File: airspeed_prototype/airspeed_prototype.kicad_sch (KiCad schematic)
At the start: 6 parts, among them J1 Conn_01x03_Pin, J3 Conn_01x06_Pin, J4 Conn_01x08_Pin, U1 ESP32-DevKitC

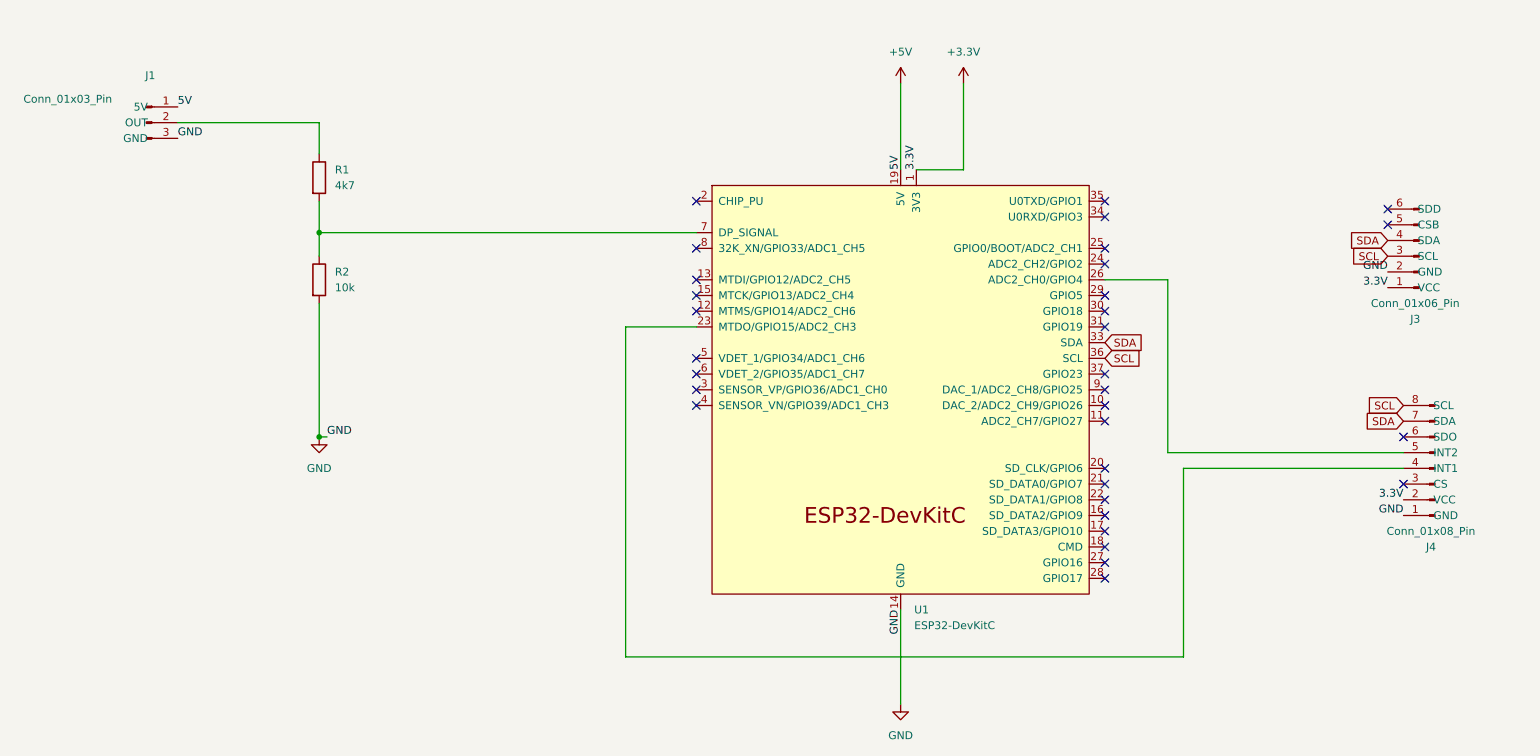
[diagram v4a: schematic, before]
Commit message: new pcb layout
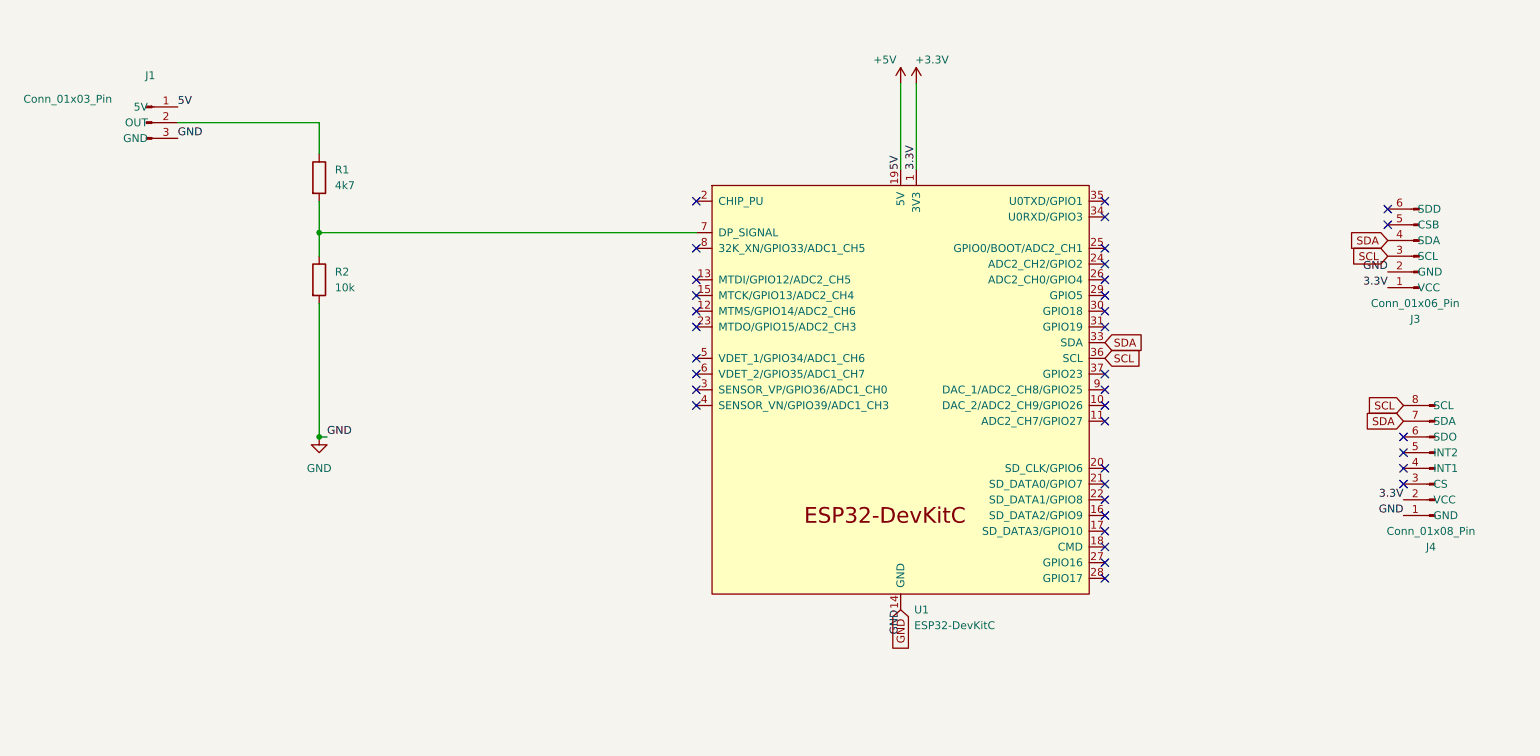
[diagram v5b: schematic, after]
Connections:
- net at U1.23 (MTDO/GPIO15/ADC2_CH3): no longer J4.4 (INT1)
- net at U1.26 (ADC2_CH0/GPIO4): no longer J4.5 (INT2)
- no-connect marks 32 -> 36
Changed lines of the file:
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@@
   (no_connect (at 129.54 50.8))
   (no_connect (at 195.58 86.36))
+  (no_connect (at 129.54 71.12))
   (no_connect (at 129.54 58.42))
   (no_connect (at 129.54 63.5))
   (no_connect (at 195.58 99.06))
+  (no_connect (at 243.84 91.44))
   (no_connect (at 243.84 96.52))
   (no_connect (at 241.3 54.61))
@@
   (no_connect (at 195.58 68.58))
   (no_connect (at 195.58 53.34))
+  (no_connect (at 243.84 93.98))
   (no_connect (at 195.58 109.22))
   (no_connect (at 195.58 104.14))
@@
   (no_connect (at 195.58 96.52))
   (no_connect (at 195.58 50.8))
+  (no_connect (at 195.58 63.5))
   (no_connect (at 195.58 60.96))
   (no_connect (at 195.58 111.76))
@@
     (stroke (width 0) (type default))
   )
-  (wire (pts (xy 208.28 124.46) (xy 118.11 124.46))
-    (stroke (width 0) (type default))
-  )
   (wire (pts (xy 129.54 55.88) (xy 68.58 55.88))
     (stroke (width 0) (type default))
   )
-  (wire (pts (xy 162.56 116.84) (xy 162.56 132.08))
-    (stroke (width 0) (type default))
-  )
   (wire (pts (xy 69.85 88.9) (xy 68.58 88.9))
     (stroke (width 0) (type default))
   )
-  (wire (pts (xy 243.84 91.44) (xy 205.74 91.44))
-    (stroke (width 0) (type default))
-  )
-  (wire (pts (xy 172.72 31.75) (xy 172.72 45.72))
-    (stroke (width 0) (type default))
-  )
-  (wire (pts (xy 205.74 91.44) (xy 205.74 63.5))
-    (stroke (width 0) (type default))
-  )
-  (wire (pts (xy 208.28 93.98) (xy 208.28 124.46))
+  (wire (pts (xy 165.1 31.75) (xy 165.1 45.72))
     (stroke (width 0) (type default))
   )
@@
     (stroke (width 0) (type default))
   )
-  (wire (pts (xy 172.72 45.72) (xy 165.1 45.72))
-    (stroke (width 0) (type default))
-  )
   (wire (pts (xy 68.58 50.8) (xy 68.58 55.88))
-    (stroke (width 0) (type default))
-  )
-  (wire (pts (xy 195.58 63.5) (xy 205.74 63.5))
-    (stroke (width 0) (type default))
-  )
-  (wire (pts (xy 118.11 124.46) (xy 118.11 71.12))
-    (stroke (width 0) (type default))
-  )
-  (wire (pts (xy 243.84 93.98) (xy 208.28 93.98))
-    (stroke (width 0) (type default))
-  )
-  (wire (pts (xy 118.11 71.12) (xy 129.54 71.12))
     (stroke (width 0) (type default))
   )
@@
     (property "Intersheetrefs" "${INTERSHEET_REFS}" (at 202.0728 76.2 0)
       (effects (font (size 1.27 1.27)) (justify left) hide)
+    )
+  )
+  (global_label "GND" (shape input) (at 162.56 116.84 270) (fields_autoplaced)
+    (effects (font (size 1.27 1.27)) (justify right))
+    (property "Intersheetrefs" "${INTERSHEET_REFS}" (at 162.56 123.6957 90)
+      (effects (font (size 1.27 1.27)) (justify right) hide)
     )
   )
@@
     )
   )
-  (symbol (lib_id "power:+3.3V") (at 172.72 31.75 0) (unit 1)
+  (symbol (lib_id "power:+3.3V") (at 165.1 31.75 0) (unit 1)
     (in_bom yes) (on_board yes) (dnp no)
-    (property "Reference" "#PWR04" (at 172.72 35.56 0)
-      (effects (font (size 1.27 1.27)) hide)
-    )
-    (property "Value" "+3.3V" (at 172.72 26.67 0)
-      (effects (font (size 1.27 1.27)))
-    )
-    (property "Footprint" "" (at 172.72 31.75 0)
-      (effects (font (size 1.27 1.27)) hide)
-    )
-    (property "Datasheet" "" (at 172.72 31.75 0)
+    (property "Reference" "#PWR04" (at 165.1 35.56 0)
+      (effects (font (size 1.27 1.27)) hide)
+    )
+    (property "Value" "+3.3V" (at 167.64 27.94 0)
+      (effects (font (size 1.27 1.27)))
+    )
+    (property "Footprint" "" (at 165.1 31.75 0)
+      (effects (font (size 1.27 1.27)) hide)
+    )
+    (property "Datasheet" "" (at 165.1 31.75 0)
       (effects (font (size 1.27 1.27)) hide)
     )
@@
   )
   (symbol (lib_id "power:+5V") (at 162.56 31.75 0) (unit 1)
-    (in_bom yes) (on_board yes) (dnp no) (fields_autoplaced)
+    (in_bom yes) (on_board yes) (dnp no)
     (property "Reference" "#PWR03" (at 162.56 35.56 0)
       (effects (font (size 1.27 1.27)) hide)
     )
-    (property "Value" "+5V" (at 162.56 26.67 0)
+    (property "Value" "+5V" (at 160.02 27.94 0)
       (effects (font (size 1.27 1.27)))
     )
@@
         )
       )
-    )
-  )
-  (symbol (lib_id "power:GND") (at 162.56 132.08 0) (unit 1)
-    (in_bom yes) (on_board yes) (dnp no) (fields_autoplaced)
-    (property "Reference" "#PWR02" (at 162.56 138.43 0)
-      (effects (font (size 1.27 1.27)) hide)
-    )
-    (property "Value" "GND" (at 162.56 137.16 0)
-      (effects (font (size 1.27 1.27)))
-    )
-    (property "Footprint" "" (at 162.56 132.08 0)
-      (effects (font (size 1.27 1.27)) hide)
-    )
-    (property "Datasheet" "" (at 162.56 132.08 0)
-      (effects (font (size 1.27 1.27)) hide)
-    )
-    (pin "1")
-    (instances
-      (project "airspeed_prototype"
-        (path "/2dd51ea1-493d-49cb-b057-63d48ce841c4"
-          (reference "#PWR02") (unit 1)
-        )
-      )
